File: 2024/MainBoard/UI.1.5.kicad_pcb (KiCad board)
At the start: 2 copper layers, 105.9 x 122.4 mm, 31 parts, among them J1 debug, Y2 Crystal_GND24

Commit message: アートワークした
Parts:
- removed Connector_Rasp1: ~, Connector_PinSocket_2.54mm:PinSocket_1x05_P2.54mm_Vertical
- removed F446RE_CN10, F446RE_CN7: ~, Connector_PinSocket_2.54mm:PinSocket_1x19_P2.54mm_Vertical
- removed MCP2562: MCP2562-E-P, Package_DIP:DIP-8_W7.62mm
- removed MCP25625: MCP25625-x-SS, Package_SO:SSOP-28_5.3x10.2mm_P0.65mm
- removed NMOS1: BSS138, NMOS:SOT95P240X111-3N
- removed TFT3: ~, Connector_PinHeader_2.54mm:PinHeader_1x04_P2.54mm_Vertical
- removed XIAO: MOUDLE-SEEEDUINO-XIAO, XIAO:MOUDLE14P-2.54-21X17.8MM
- removed Y2: Crystal_GND24, Oscillator:Oscillator_SMD_EuroQuartz_XO32-4Pin_3.2x2.5mm_HandSoldering
- added C3: 4.7uF, Capacitor_SMD:C_0402_1005Metric, B.Cu at (225.8, 67.5)
- added C4: 0.1uF, Capacitor_SMD:C_0402_1005Metric, B.Cu at (223.5, 68.0)
- added C5: 0.1uF, Capacitor_SMD:C_0402_1005Metric, B.Cu at (223.5, 66.7)
- added C6: 0.1uF, Capacitor_SMD:C_0402_1005Metric, B.Cu at (227.6, 68.5)
- added C7: 0.1uF, Capacitor_SMD:C_0402_1005Metric, B.Cu at (227.6, 64.9)
- added C8: 0.1uF, Capacitor_SMD:C_0402_1005Metric, B.Cu at (227.6, 69.7)
- added C9: 0.1uF, Capacitor_SMD:C_0402_1005Metric, B.Cu at (222.6, 39.6)
- added D6: LED_Ras2, LED_SMD:LED_0603_1608Metric_Pad1.05x0.95mm_HandSolder, F.Cu at (198.8, 144.5)
- added D7: LED_USB, LED_SMD:LED_0603_1608Metric_Pad1.05x0.95mm_HandSolder, F.Cu at (200.4, 36.3)
- added D8: LED_volt, LED_SMD:LED_0603_1608Metric_Pad1.05x0.95mm_HandSolder, F.Cu at (200.4, 43.7)
- added D9: LED_Debug, LED_SMD:LED_0603_1608Metric_Pad1.05x0.95mm_HandSolder, F.Cu at (200.4, 38.8)
- added J2: fan, pad:fan_pad, F.Cu at (204.7, 85.2)
- added J3: Debug, Connector_PinSocket_2.54mm:PinSocket_1x07_P2.54mm_Vertical, F.Cu at (240.9, 81.0)
- added J4: USB_C_Receptacle_USB2.0_16P, Connector_USB:USB_C_Receptacle_G-Switch_GT-USB-7010ASV, F.Cu at (234.1, 38.1)
- added J5: Can_debug, Connector_PinSocket_2.54mm:PinSocket_1x03_P2.54mm_Vertical, F.Cu at (236.2, 103.3)
- added Q1: NMOS, NMOS:SOT95P240X111-3N, F.Cu at (212.3, 128.3)
- added R10: 120, Resistor_SMD:R_0402_1005Metric, F.Cu at (233.7, 92.2)
- added R11: 120, Resistor_SMD:R_0402_1005Metric, F.Cu at (203.8, 36.3)
- added R12: 5.1k, Resistor_SMD:R_0402_1005Metric, B.Cu at (235.7, 37.5)
- added R13: 5.1k, Resistor_SMD:R_0402_1005Metric, B.Cu at (233.0, 37.5)
- added R14: 120, Resistor_SMD:R_0402_1005Metric, F.Cu at (204.0, 38.9)
- added R15: R, Resistor_SMD:R_0402_1005Metric, F.Cu at (202.5, 141.9)
- added SW1: SW_Coded_SH-7050, Button_Switch_SMD:Nidec_Copal_SH-7010A, F.Cu at (210.3, 143.2)
- added SW2: Ras_1, Button_Switch_SMD:SW_SPST_Omron_B3FS-100xP, F.Cu at (221.0, 143.2)
- added SW3: Ras_2, Button_Switch_SMD:SW_SPST_Omron_B3FS-100xP, F.Cu at (232.9, 143.2)
- added SW4: NRST, Button_Switch_SMD:SW_SPST_Omron_B3FS-100xP, F.Cu at (222.6, 39.1)
- added SW5: Boot, Button_Switch_THT:SW_Slide-03_Wuerth-WS-SLTV_10x2.5x6.4_P2.54mm, F.Cu at (211.3, 39.1)
- added U1: MOUDLE-SEEEDUINO-XIAO, XIAO:MOUDLE14P-SMD-2.54-21X17.8MM, F.Cu at (209.6, 70.1)
- added U2: MCP2562-E-P, Package_DIP:DIP-8_W7.62mm, F.Cu at (230.3, 82.2)
- added U3: CH340E, Package_SO:MSOP-10_3x3mm_P0.5mm, F.Cu at (241.3, 50.8)
- added U4: STM32F446RETx, Package_QFP:LQFP-64_10x10mm_P0.5mm, F.Cu at (226.1, 67.3)
- C1: value C -> 4.7u; footprint Capacitor_THT:C_Disc_D3.8mm_W2.6mm_P2.50mm -> Capacitor_SMD:C_0402_1005Metric
- C2: value C -> 0.1uF; footprint Capacitor_THT:C_Disc_D3.8mm_W2.6mm_P2.50mm -> Capacitor_SMD:C_0402_1005Metric
- Connector_Sub1: footprint Connector_PinSocket_2.54mm:PinSocket_1x06_P2.54mm_Vertical -> Connector_JST:JST_XH_S6B-XH-A_1x06_P2.50mm_Horizontal
- D1: value LED -> LED_main; footprint LED_THT:LED_D3.0mm -> LED_SMD:LED_0603_1608Metric_Pad1.05x0.95mm_HandSolder
- D2: value D -> SS210; footprint Diode_THT:D_A-405_P7.62mm_Horizontal -> Diode_SMD:D_SMA; moved to B.Cu
- D3: value D -> SS210; footprint Diode_THT:D_A-405_P7.62mm_Horizontal -> Diode_SMD:D_SMA
- D4: value D -> SS210; footprint Diode_THT:D_A-405_P12.70mm_Horizontal -> Diode_SMD:D_SMA
- D5: value LED -> LED_Ras1; footprint LED_THT:LED_D3.0mm -> LED_SMD:LED_0603_1608Metric_Pad1.05x0.95mm_HandSolder
- J1: value debug -> Raspberry_Pi_2_3; footprint Connector_PinSocket_2.54mm:PinSocket_1x02_P2.54mm_Vertical -> Connector_PinSocket_2.54mm:PinSocket_2x20_P2.54mm_Vertical; moved to B.Cu
- R1, R3, R4, R5: footprint Resistor_THT:R_Axial_DIN0309_L9.0mm_D3.2mm_P15.24mm_Horizontal -> Resistor_SMD:R_0402_1005Metric
- R2: value 600R -> 300; footprint Resistor_THT:R_Axial_DIN0309_L9.0mm_D3.2mm_P15.24mm_Horizontal -> Resistor_SMD:R_0402_1005Metric
- R6, R7: footprint Resistor_THT:R_Axial_DIN0207_L6.3mm_D2.5mm_P15.24mm_Horizontal -> Resistor_SMD:R_0402_1005Metric; moved to B.Cu
- R8: footprint Resistor_THT:R_Axial_DIN0207_L6.3mm_D2.5mm_P15.24mm_Horizontal -> Resistor_SMD:R_0402_1005Metric
- R9: value 120 -> R; footprint Resistor_THT:R_Axial_DIN0309_L9.0mm_D3.2mm_P15.24mm_Horizontal -> Resistor_SMD:R_0402_1005Metric
- TFT1: footprint Connector_PinHeader_2.54mm:PinHeader_1x08_P2.54mm_Vertical -> Connector_PinSocket_2.54mm:PinSocket_1x08_P2.54mm_Vertical
- TFT2: footprint Connector_PinHeader_2.54mm:PinHeader_1x04_P2.54mm_Vertical -> Connector_PinSocket_2.54mm:PinSocket_1x04_P2.54mm_Vertical
- moved D5 120.4 mm to (198.8, 141.9), turned to 180 degrees
- moved Connector_Sub1 118.7 mm to (235.1, 124.4), turned to 90 degrees
- moved C2 116.4 mm to (242.7, 56.6)
- moved R9 115.4 mm to (202.5, 144.6), turned to 0 degrees
- moved C1 110.4 mm to (234.5, 71.4), turned to 45 degrees
- moved R2 105.8 mm to (203.8, 43.7), turned to 180 degrees
- moved R7 105.0 mm to (232.9, 78.9)
- moved R6 93.3 mm to (232.9, 76.6)
- moved R8 91.5 mm to (203.8, 41.1)
- moved R1 85.2 mm to (214.2, 124.8), turned to 180 degrees
- moved LS1 83.3 mm to (222.2, 129.2), turned to 180 degrees
- moved D1 79.4 mm to (200.4, 41.2), turned to 0 degrees
- moved D2 76.7 mm to (227.7, 77.7), turned to 180 degrees
- moved TFT2 70.8 mm to (210.3, 48.3)
- moved TFT1 70.8 mm to (233.1, 48.3)
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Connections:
- C1 pad 1: +5V -> Net-(U4-VCAP_1)
- C2 pad 2: +3.3V -> Net-(U3-V3)
- D1 pad 1: +5V -> GND
- D2 pad 2: UI_Audio -> Volt_SIG
- D3 pad 1: Net-(D2-K) -> UI_Audio
- D3 pad 2: Ras_Audio -> Net-(D3-A)
- D4 pad 1: Volt_SIG -> Ras_Audio
- D4 pad 2: Net-(D4-A) -> Net-(D3-A)
- D5 pad 2: Main_LED -> LED1
- J1 pad 1: CANH -> +3.3V
- J1 pad 2: CANL -> +5V
- R2 pad 2: Net-(D1-A) -> Net-(D8-A)
- R3 pad 1: CANH -> Net-(SW5-B)
- R3 pad 2: CANL -> GND
- R6 pad 1: Net-(D4-A) -> Net-(D2-K)
- R7 pad 2: Net-(D4-A) -> Net-(D2-K)
- R8 pad 1: Net-(D5-K) -> Main_LED
- R8 pad 2: GND -> Net-(D1-A)
- R9 pad 1: CANH -> Net-(D6-K)
- R9 pad 2: CANL -> GND
- TFT1 pad 1: 3.3V -> +3.3V
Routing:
- net GND: track 494.5 -> 135.7 mm, vias 5 -> 23
- net +3.3V: track 112.8 -> 302.4 mm, vias 1 -> 13
- net CANH: track 150.6 -> 30.5 mm, vias 5 -> 0
- net NRST: track 0.00 -> 117.3 mm, vias 0 -> 6
- net CANL: track 143.3 -> 33.4 mm, vias 6 -> 0
- net 3.3V: track 70.0 -> 0.00 mm
- net R2: track 0.00 -> 66.6 mm, vias 0 -> 4
- net SW2: track 0.00 -> 65.9 mm
- net R3: track 0.00 -> 65.7 mm, vias 0 -> 3
- net Main_LED: track 156.0 -> 92.1 mm, vias 3 -> 4
- net Net-(SW5-B): track 0.00 -> 62.7 mm, vias 0 -> 2
- net R4: track 0.00 -> 59.1 mm, vias 0 -> 3
- net SW1: track 0.00 -> 58.5 mm
- net Volt_SIG: track 63.8 -> 5.86 mm
- net ST_TX: track 0.00 -> 57.3 mm, vias 0 -> 2
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- added copper zone on In1.Cu, net +3.3V
- added copper zone on In2.Cu, net GND
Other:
- board size 105.9 x 122.4 mm -> 64.3 x 113.9 mm
- copper layers 2 -> 4
- board text removed: "Riku"
- board text removed: "検証用1"

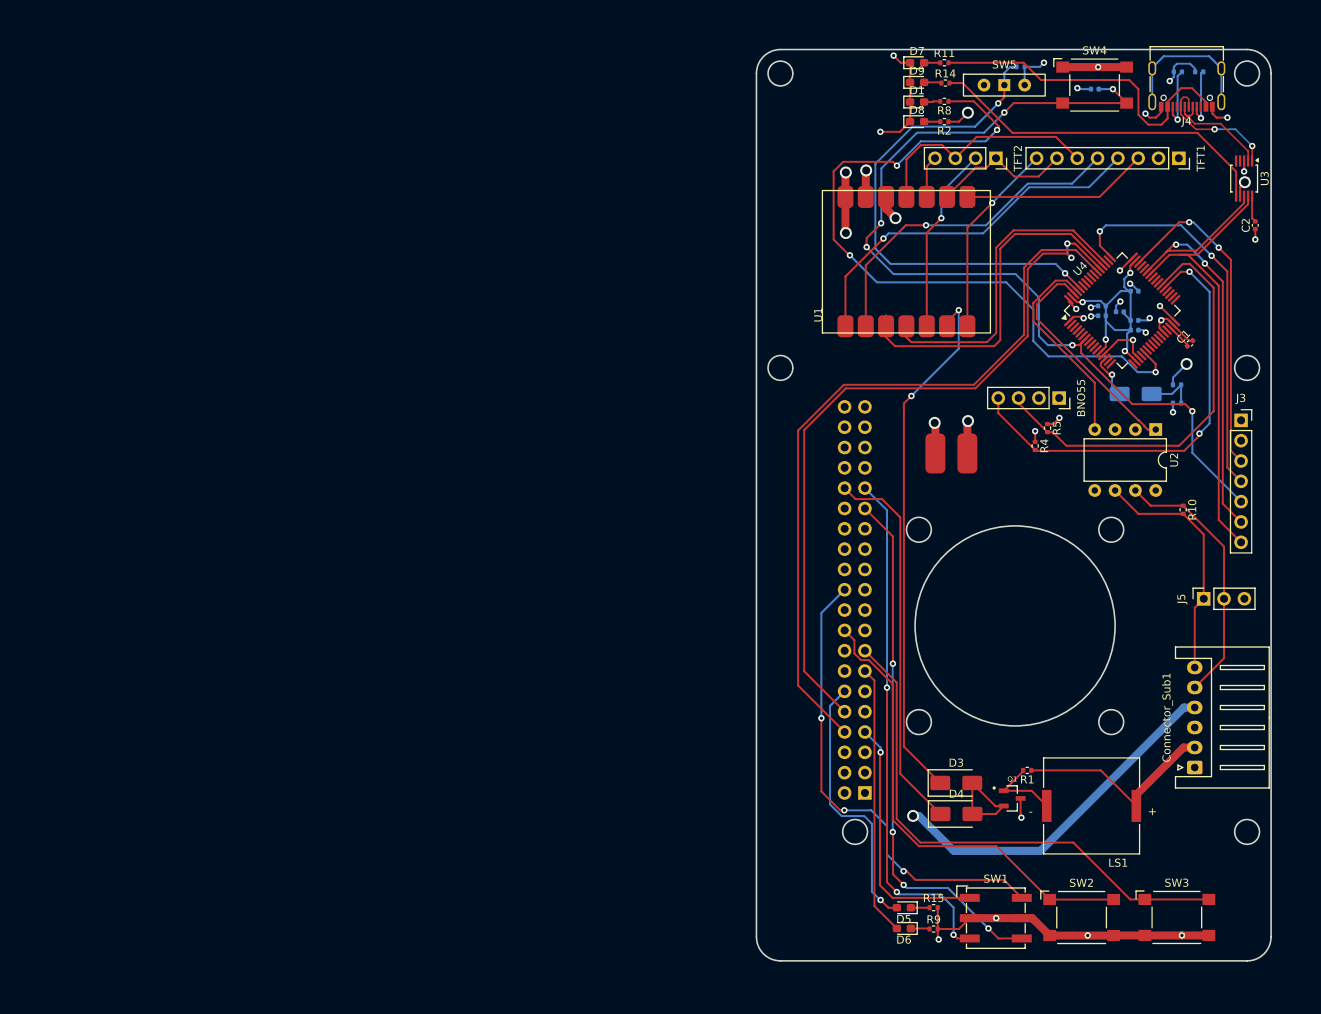
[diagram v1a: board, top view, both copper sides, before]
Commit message: 最終版
未実装：canでの通信(mainとxiao）
dc-dc
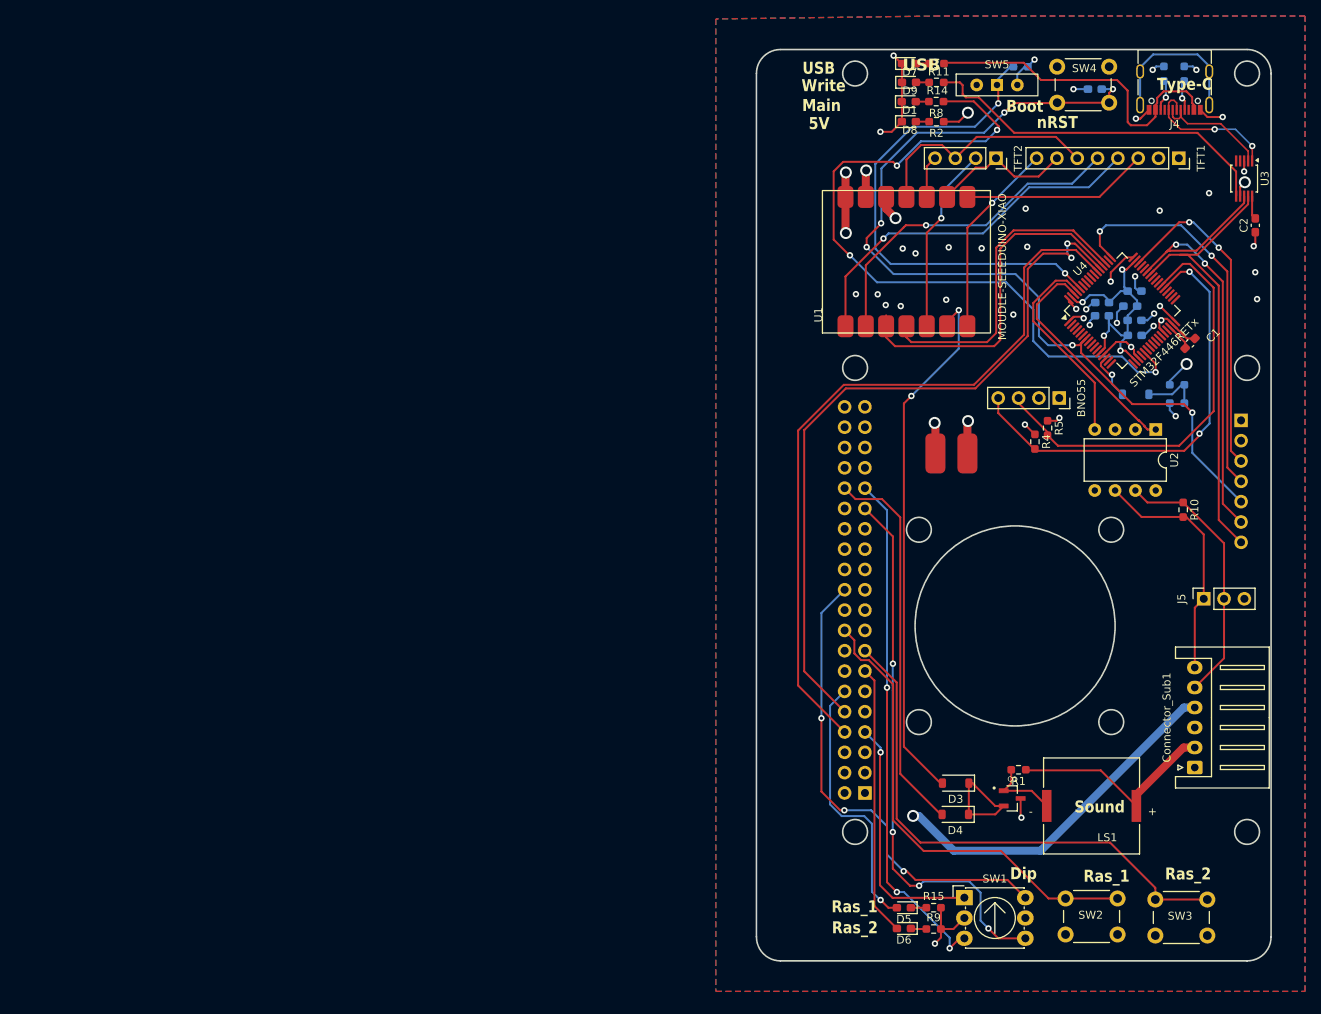
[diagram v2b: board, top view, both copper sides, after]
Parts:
- C1, C2, C4, C5, C6, C7, C8, C9: footprint Capacitor_SMD:C_0402_1005Metric -> Capacitor_SMD:C_0603_1608Metric_Pad1.08x0.95mm_HandSolder
- C3: value 4.7uF -> 4.7u; footprint Capacitor_SMD:C_0402_1005Metric -> Capacitor_SMD:C_0603_1608Metric_Pad1.08x0.95mm_HandSolder
- D2, D3, D4: value SS210 -> 1N4148W; footprint Diode_SMD:D_SMA -> Diode_SMD:D_SOD-123
- J3: moved to B.Cu
- R1: value 1kR -> 1k; footprint Resistor_SMD:R_0402_1005Metric -> Resistor_SMD:R_0603_1608Metric_Pad0.98x0.95mm_HandSolder
- R10, R12, R13, R4, R5, R6, R7: footprint Resistor_SMD:R_0402_1005Metric -> Resistor_SMD:R_0603_1608Metric_Pad0.98x0.95mm_HandSolder
- R11, R14: value 120 -> 470; footprint Resistor_SMD:R_0402_1005Metric -> Resistor_SMD:R_0603_1608Metric_Pad0.98x0.95mm_HandSolder
- R15, R8, R9: value R -> 300; footprint Resistor_SMD:R_0402_1005Metric -> Resistor_SMD:R_0603_1608Metric_Pad0.98x0.95mm_HandSolder
- R2: value 300 -> 470; footprint Resistor_SMD:R_0402_1005Metric -> Resistor_SMD:R_0603_1608Metric_Pad0.98x0.95mm_HandSolder
- R3: value 120 -> 300; footprint Resistor_SMD:R_0402_1005Metric -> Resistor_SMD:R_0603_1608Metric_Pad0.98x0.95mm_HandSolder
- SW1: value SW_Coded_SH-7050 -> SW_Coded_SH-7070; footprint Button_Switch_SMD:Nidec_Copal_SH-7010A -> Button_Switch_THT:Nidec_Copal_SH-7010C
- SW2, SW3, SW4: footprint Button_Switch_SMD:SW_SPST_Omron_B3FS-100xP -> Button_Switch_THT:SW_PUSH_6mm_H7.3mm
- moved SW4 5.22 mm to (217.9, 36.8)
- moved SW1 4.69 mm to (206.3, 140.7)
- moved SW3 3.50 mm to (230.2, 140.9)
- moved SW2 3.11 mm to (219.0, 140.8)
- moved R12 1.90 mm to (233.8, 37.7), turned to 90 degrees
- moved R13 1.77 mm to (231.3, 37.7), turned to 90 degrees
- moved J4 1.56 mm to (232.6, 38.5)
- moved C3 1.47 mm to (227.1, 66.8)
- moved R14 1.12 mm to (202.8, 38.8)
- moved R1 1.09 mm to (213.1, 124.7)
- moved D1 1.04 mm to (199.4, 41.2)
- moved D8 1.03 mm to (199.4, 43.7)
- moved R8 1.03 mm to (202.8, 41.2)
- moved D7 1.02 mm to (199.4, 36.4)
- moved D9 1.01 mm to (199.4, 38.8)
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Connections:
- D2 pad 1: Net-(D2-K) -> Volt_SIG
- D2 pad 2: Volt_SIG -> Net-(D2-A)
- D3 pad 1: UI_Audio -> Net-(D3-K)
- D3 pad 2: Net-(D3-A) -> UI_Audio
- D4 pad 1: Ras_Audio -> Net-(D3-K)
- D4 pad 2: Net-(D3-A) -> Ras_Audio
- Q1 pad 2: Net-(D3-A) -> Net-(D3-K)
- R6 pad 1: Net-(D2-K) -> Net-(D2-A)
- R7 pad 2: Net-(D2-K) -> Net-(D2-A)
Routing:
- net GND: track 135.7 -> 92.6 mm, vias 23 -> 36
- net Net-(D3-K): track 0.00 -> 14.3 mm
- net Net-(D3-A): track 13.3 -> 0.00 mm
- net +3.3V: track 302.4 -> 311.4 mm
- net Net-(D2-A): track 0.00 -> 7.21 mm
- net Net-(D2-K): track 6.44 -> 0.00 mm
- net Net-(J4-CC2): track 8.05 -> 3.97 mm
- net Net-(J4-CC1): track 7.47 -> 3.84 mm
- net NRST: track 117.3 -> 114.6 mm
- net R2: track 66.6 -> 69.1 mm
- net +5V: track 247.6 -> 246.1 mm
- net Net-(U3-TNOW): track 43.5 -> 44.9 mm
- net D+: track 16.4 -> 17.8 mm
- net D-: track 14.0 -> 15.3 mm
- net unconnected-(J4-SHIELD-PadS1): track 18.3 -> 19.5 mm
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- added copper zone on In1.Cu, net +5V
- added copper zone on B.Cu, net GND
- added copper zone on F.Cu, net GND
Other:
- outline, holes or cut-outs redrawn
- board text added: "5V"
- board text added: "Boot"
- board text added: "Dip"
- board text added: "Main"
- board text added: "Ras_1"
- board text added: "Ras_2"
- board text added: "Sound"
- board text added: "Type-C"
- board text added: "USB"
- board text added: "Write"
- board text added: "nRST"

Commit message: 発注版
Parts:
- added C10: 0.1u, Capacitor_SMD:C_0603_1608Metric_Pad1.08x0.95mm_HandSolder, B.Cu at (187.0, 126.5)
- added C11: 0.1u, Capacitor_SMD:C_0603_1608Metric_Pad1.08x0.95mm_HandSolder, B.Cu at (206.0, 133.2)
- added C12: 0.1uF, Capacitor_SMD:C_0603_1608Metric_Pad1.08x0.95mm_HandSolder, B.Cu at (239.5, 46.7)
- added C13: 0.1uF, Capacitor_SMD:C_0603_1608Metric_Pad1.08x0.95mm_HandSolder, B.Cu at (225.1, 85.9)
- added C14: 0.1u, Capacitor_SMD:C_0603_1608Metric_Pad1.08x0.95mm_HandSolder, B.Cu at (192.4, 56.1)
- added C15: 0.1u, Capacitor_SMD:C_0603_1608Metric_Pad1.08x0.95mm_HandSolder, B.Cu at (187.0, 129.7)
- added C16: 0.1u, Capacitor_SMD:C_0603_1608Metric_Pad1.08x0.95mm_HandSolder, B.Cu at (204.0, 133.2)
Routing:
- net GND: track 92.6 -> 108.9 mm, vias 36 -> 41
- net +5V: track 246.1 -> 258.2 mm, vias 7 -> 11
- net +3.3V: track 311.4 -> 309.3 mm
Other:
- outline, holes or cut-outs redrawn
- board text added: "15V"
- board text added: "3.3V"
- board text added: "CANH"
- board text added: "CANL"
- board text added: "Designed by Riku Miyazaki"
- board text added: "GND"
- board text added: "Main v.1.5"
- board text added: "NRST"
- board text added: "RX"
- board text added: "SWCLK"
- board text added: "SWDIO"
- board text added: "TX"
